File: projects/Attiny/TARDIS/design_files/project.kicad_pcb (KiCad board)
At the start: 2 copper layers, 25.4 x 48.3 mm, 13 parts, among them CON1 AVR-ISP-6, IC1 ATTINY85, SW1 TOUCH, SW2 ON

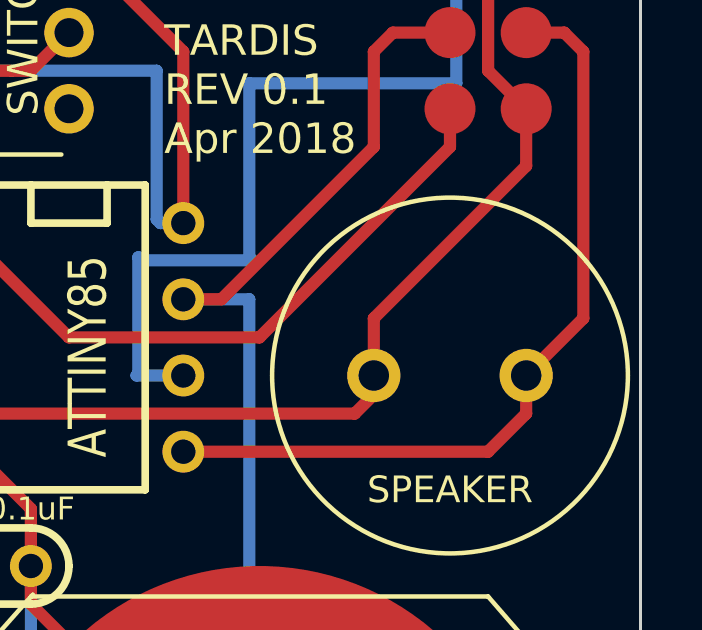
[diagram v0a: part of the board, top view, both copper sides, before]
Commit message: Taris silk screen update
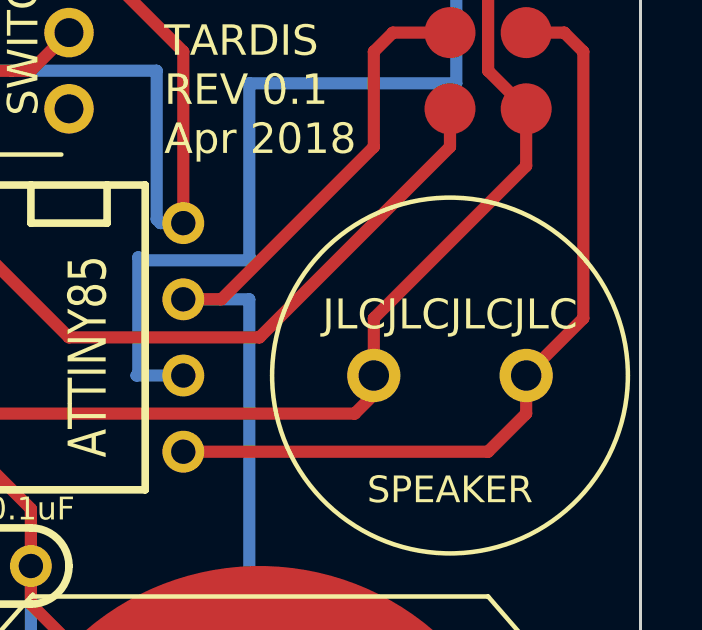
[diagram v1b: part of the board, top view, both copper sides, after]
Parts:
- removed the LOGO at (132.1, 102.9)
- removed the LOGO at (142.2, 102.9)
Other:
- board text added: "JLCJLCJLCJLC"
